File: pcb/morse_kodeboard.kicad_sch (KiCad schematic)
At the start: 7 parts, among them SW1 SW_DPST

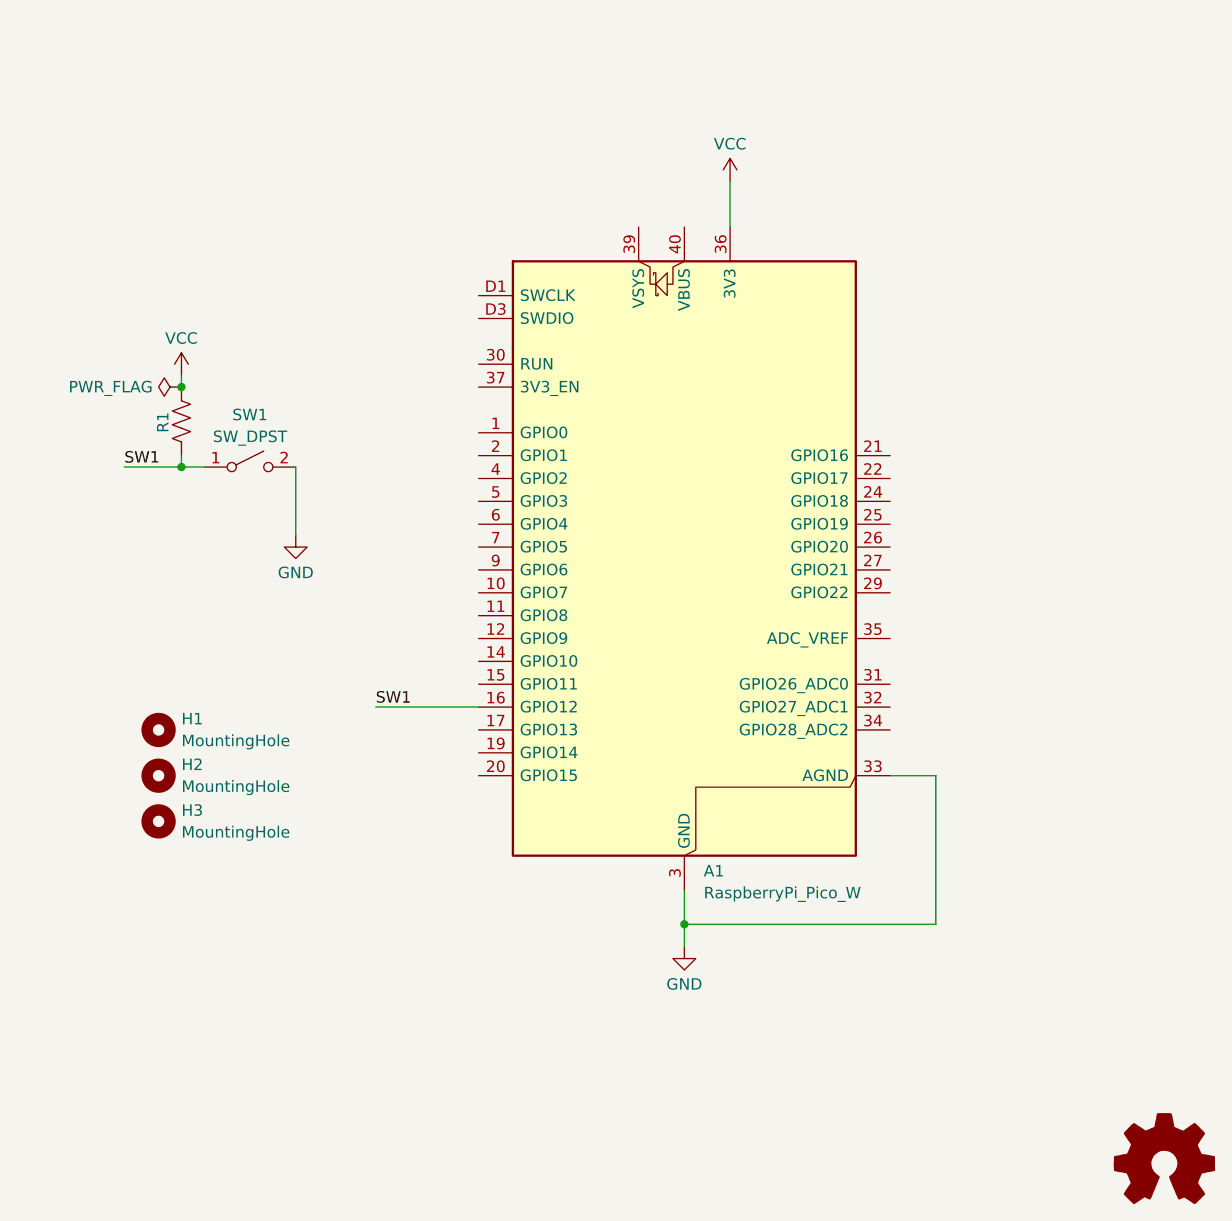
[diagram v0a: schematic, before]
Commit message: Make PCB single button
Signed-off-by: William Hart <391950+will-hart@users.noreply.github.com>
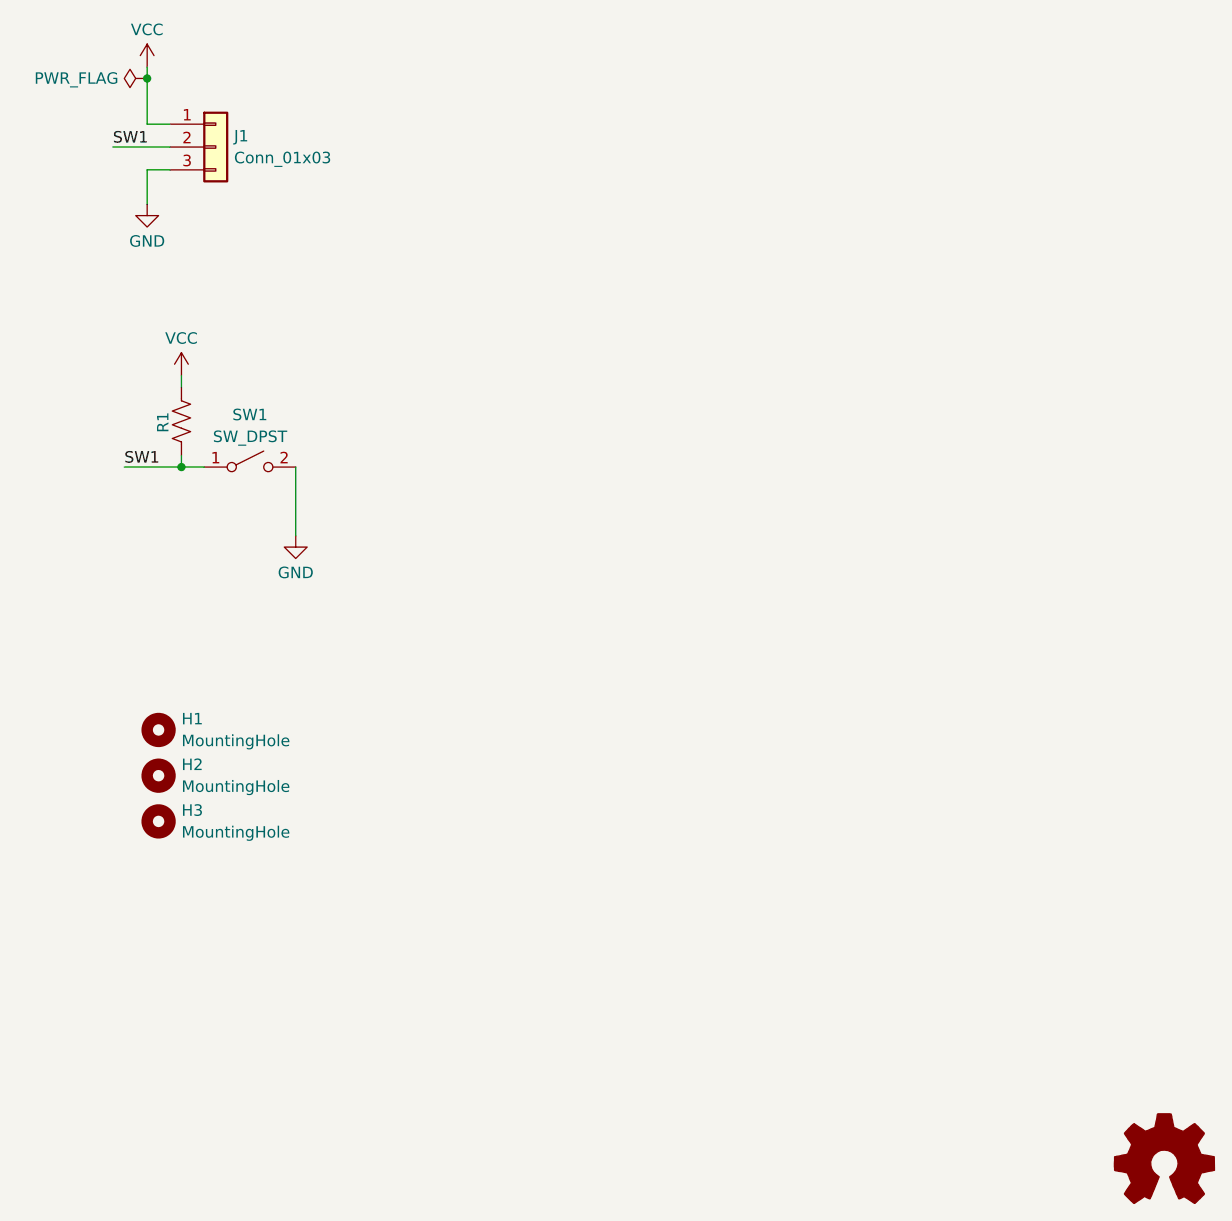
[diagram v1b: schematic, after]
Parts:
- removed A1: RaspberryPi_Pico_W, Module:RaspberryPi_Pico_W_SMD_HandSolder, symbol MCU_Module:RaspberryPi_Pico_W_Debug
- added J1: Conn_01x03, Connector_JST:JST_PH_S3B-PH-K_1x03_P2.00mm_Horizontal, symbol Connector_Generic:Conn_01x03
- H1, H2, H3: footprint MountingHole:MountingHole_3.2mm_M3 -> MountingHole:MountingHole_2.2mm_M2
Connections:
- net GND: now also J1.3 (Pin_3)
- net SW1: now also J1.2 (Pin_2)
- net VCC: now also J1.1 (Pin_1)

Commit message: Update PCB files with three buttons.
Sent off to fab as r1!

Signed-off-by: William Hart <391950+will-hart@users.noreply.github.com>
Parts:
- added H4: MountingHole, MountingHole:MountingHole_2.2mm_M2, symbol Mechanical:MountingHole
- added R2, R3: R_US, Resistor_SMD:R_0805_2012Metric_Pad1.20x1.40mm_HandSolder, symbol Device:R_US
- added SW2, SW3: SW_DPST, PCM_Switch_Keyboard_Hotswap_Kailh:SW_Hotswap_Kailh_MX_1.00u, symbol Switch:SW_SPST
- J1: footprint Connector_JST:JST_PH_S3B-PH-K_1x03_P2.00mm_Horizontal -> Connector_JST:JST_PH_S5B-PH-K_1x05_P2.00mm_Horizontal; symbol Connector_Generic:Conn_01x03 -> Connector_Generic:Conn_01x05
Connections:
- net GND: now also J1.5 (Pin_5), SW2.2 (B), SW3.2 (B); no longer J1.3 (Pin_3)
- net VCC: now also R2.1, R3.1
- new net SW2: J1.3 (Pin_3), R2.2, SW2.1 (A)
- new net SW3: J1.4 (Pin_4), R3.2, SW3.1 (A)
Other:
- moved on the sheet: H1, H2, H3
